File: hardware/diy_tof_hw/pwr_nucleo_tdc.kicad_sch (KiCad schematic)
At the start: 20 parts, among them IC1 TDC7200PWR, IC2 TDC7200PWR, J1 Conn_01x02_Pin, J2 Conn_01x03_Pin, J3 Conn_01x02_Pin, SW1 SW_Nidec_CAS-120A1, U1 NUCLEO-F042K6, X1 SG-5032CAN

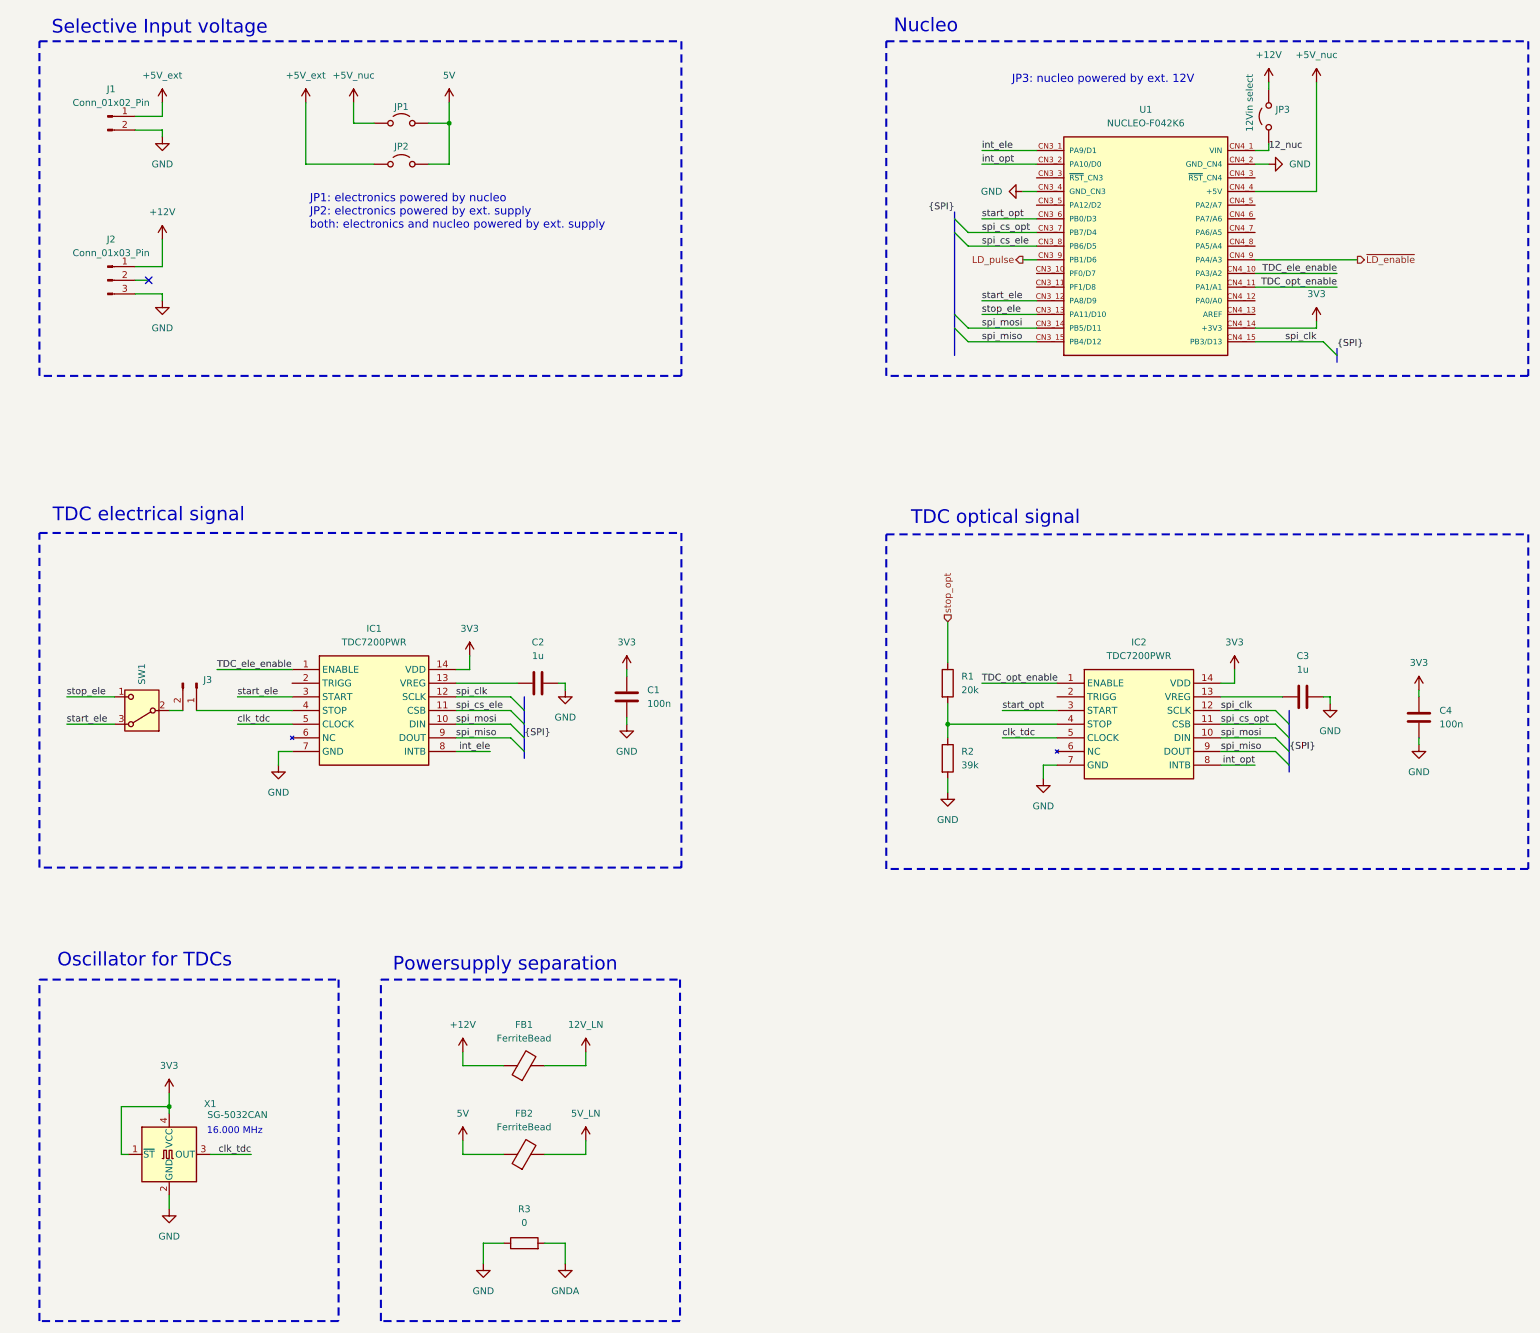
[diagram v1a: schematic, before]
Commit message: [hardware] added various testpoints, some minor other fixes on the layout (designators)
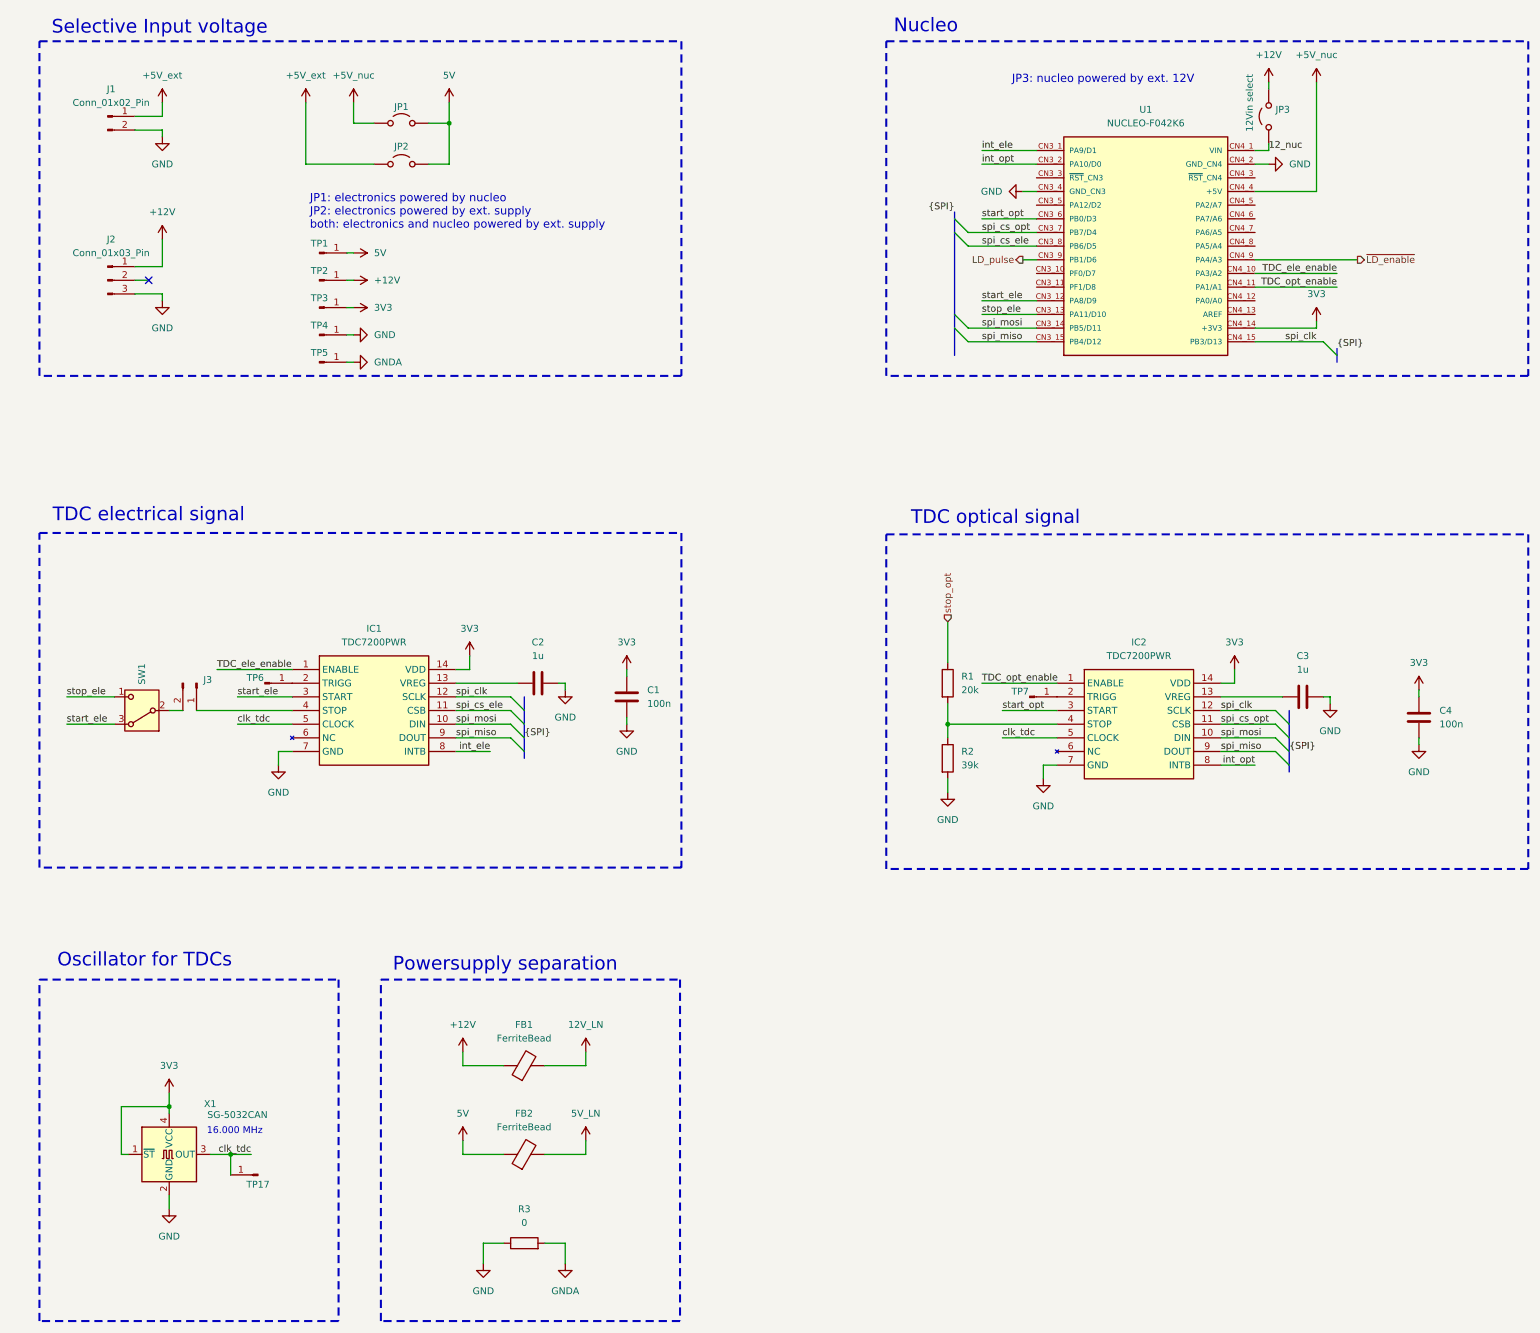
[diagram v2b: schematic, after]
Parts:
- added TP1, TP17, TP2, TP3, TP4, TP5, TP6, TP7: Conn_01x01_Pin, Connector_PinHeader_2.54mm:PinHeader_1x01_P2.54mm_Vertical, symbol Connector:Conn_01x01_Pin
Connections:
- net +12V: now also TP2.1 (Pin_1)
- net 3V3: now also TP3.1 (Pin_1)
- net 5V: now also TP1.1 (Pin_1)
- net GND: now also TP4.1 (Pin_1)
- net GNDA: now also TP5.1 (Pin_1)
- net clk_tdc: now also TP17.1 (Pin_1)
- net at IC1.2 (TRIGG): now also TP6.1 (Pin_1)
- net at IC2.2 (TRIGG): now also TP7.1 (Pin_1)

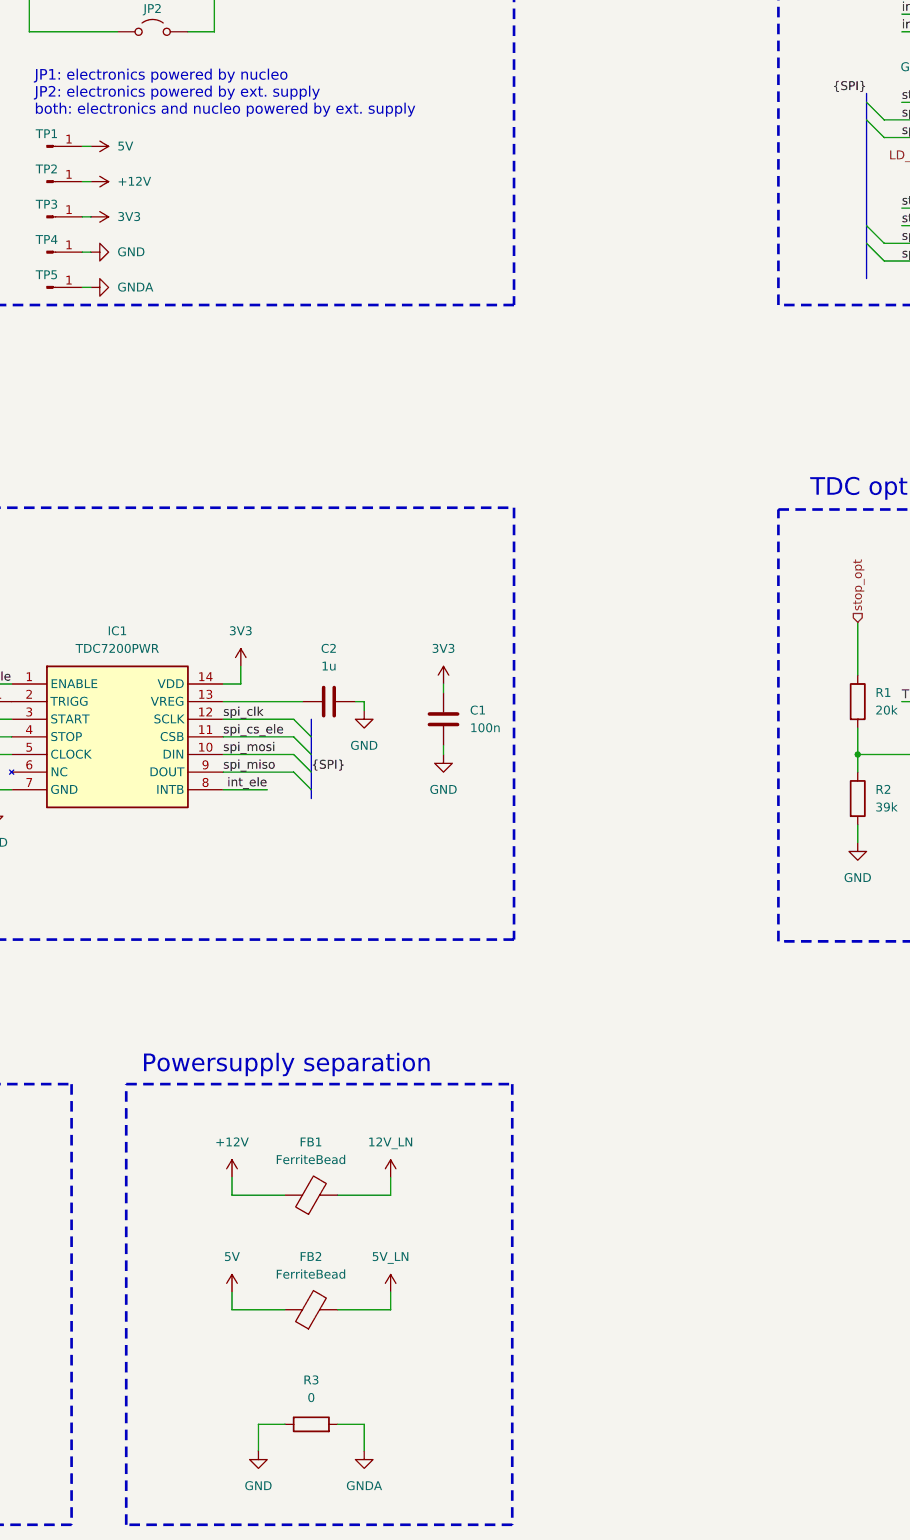
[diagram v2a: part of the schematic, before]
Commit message: [hardware] added mounting holes, reannotated some caps, started placement of the TIA part
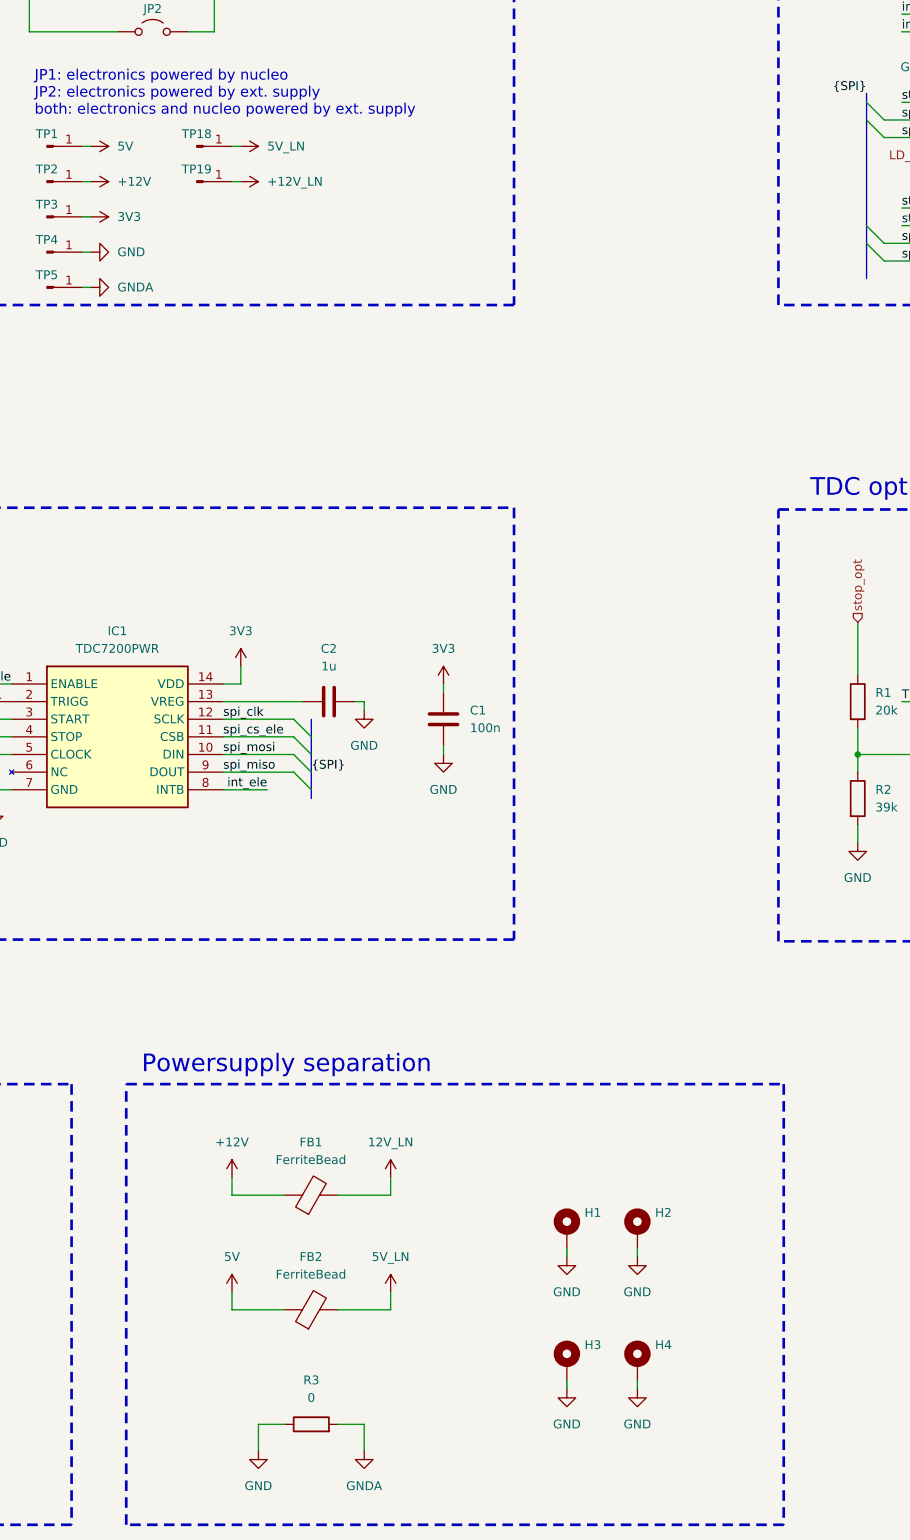
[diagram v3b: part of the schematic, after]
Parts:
- added H1, H2, H3, H4: MountingHole_Pad, MountingHole:MountingHole_3.2mm_M3_DIN965_Pad_TopBottom, symbol Mechanical:MountingHole_Pad
- added TP18, TP19: Conn_01x01_Pin, Connector_PinHeader_2.54mm:PinHeader_1x01_P2.54mm_Vertical, symbol Connector:Conn_01x01_Pin
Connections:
- net 5V_LN: now also TP18.1 (Pin_1)
- net GND: now also H1.1, H2.1, H3.1, H4.1
- new net +12V_LN: TP19.1 (Pin_1)

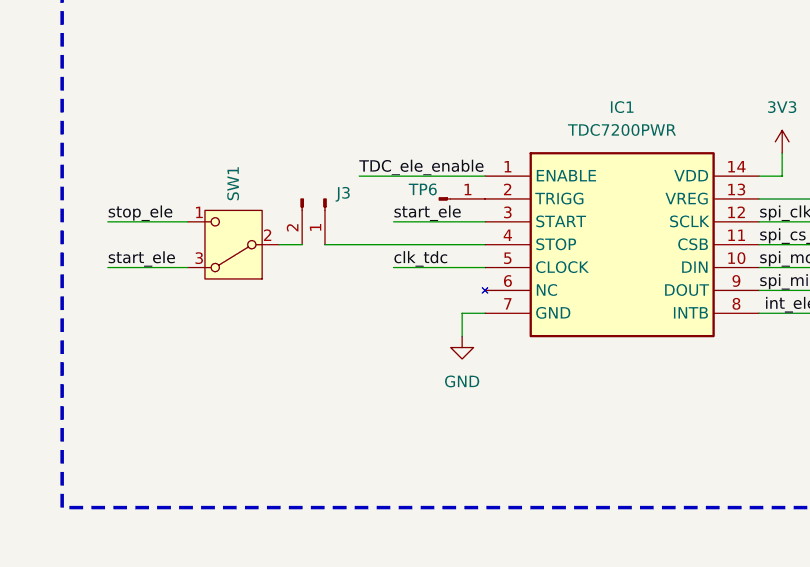
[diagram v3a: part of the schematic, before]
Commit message: [hardware] added missing TP20
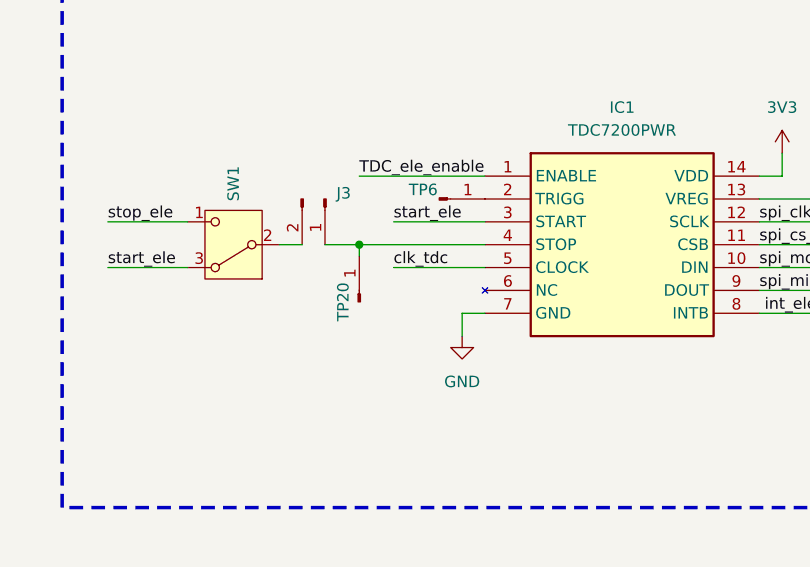
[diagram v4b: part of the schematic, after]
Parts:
- added TP20: Conn_01x01_Pin, Connector_PinHeader_2.54mm:PinHeader_1x01_P2.54mm_Vertical, symbol Connector:Conn_01x01_Pin
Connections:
- net at IC1.4 (STOP), J3.1 (Pin_1): now also TP20.1 (Pin_1)
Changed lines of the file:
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@@
 	)
 	(junction
+		(at 66.04 149.86)
+		(diameter 0)
+		(color 0 0 0 0)
+	)
+	(junction
 		(at 68.58 232.41)
 		(diameter 0)
@@
 	(wire
 		(pts
+			(xy 66.04 149.86) (xy 80.01 149.86)
+		)
+		(stroke
+			(width 0)
+			(type default)
+		)
+	)
+	(wire
+		(pts
 			(xy 64.77 232.41) (xy 68.58 232.41)
 		)
@@
 	(wire
 		(pts
-			(xy 62.23 149.86) (xy 80.01 149.86)
+			(xy 62.23 149.86) (xy 66.04 149.86)
 		)
 		(stroke
@@
 	(wire
 		(pts
+			(xy 66.04 151.13) (xy 66.04 149.86)
+		)
+		(stroke
+			(width 0)
+			(type default)
+		)
+	)
+	(wire
+		(pts
 			(xy 212.09 149.86) (xy 222.25 149.86)
 		)
@@
 					(unit 1)
 				)
+			)
+		)
+	)
+	(symbol
+		(lib_id "Connector:Conn_01x01_Pin")
+		(at 66.04 156.21 90)
+		(unit 1)
+		(exclude_from_sim no)
+		(in_bom yes)
+		(on_board yes)
+		(dnp no)
+		(property "Reference" "TP20"
+			(at 64.262 156.21 0)
+			(effects
+				(font
+					(size 1.27 1.27)
+				)
+			)
+		)
+		(property "Value" "Conn_01x01_Pin"
+			(at 63.5 155.575 0)
+			(effects
+				(font
+					(size 1.27 1.27)
+				)
+				(hide yes)
+			)
+		)
+		(property "Footprint" "Connector_PinHeader_2.54mm:PinHeader_1x01_P2.54mm_Vertical"
+			(at 66.04 156.21 0)
+			(effects
+				(font
+					(size 1.27 1.27)
+				)
+				(hide yes)
+			)
+		)
+		(property "Datasheet" "~"
+			(at 66.04 156.21 0)
+			(effects
+				(font
+					(size 1.27 1.27)
+				)
+				(hide yes)
+			)
+		)
+		(property "Description" "Generic connector, single row, 01x01, script generated"
+			(at 66.04 156.21 0)
+			(effects
+				(font
+					(size 1.27 1.27)
+				)
+				(hide yes)
+			)
+		)
+		(pin "1"
+		)
+		(instances
+			(project "diy_tof_hw"
+				(path "/0f7bf370-0a80-4101-a61d-d850fd66ab1d/e3345fca-f581-4274-8897-90c8927ce695"
+					(reference "TP20")
+					(unit 1)
+				)
